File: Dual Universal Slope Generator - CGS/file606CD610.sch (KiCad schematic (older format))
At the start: 81 parts, among them J10 TRIG_IN_B, J11 IN_B, J12 1V/OCT_B, J13 DC_OUT_B, J14 AC_COUPLED_OUT_B, J15 END_OUT_B, J16 BIPOLAR_OUT_B, J22 CV_POT_2_B, J23 FALL_POT_B, J24 RISE_POT_B, J25 SW_RISE_B, J26 SW_FALL_B, J28 LED_B, J9 CV_IN_B, Q10 2N3906, Q11 2N3904, Q12 BC547, Q7 2N3904, Q8 2N3906, Q9 2N3906, SW2 SW_SPDT_MSM, U4 LF353, U5 TL072, U6 LM3900

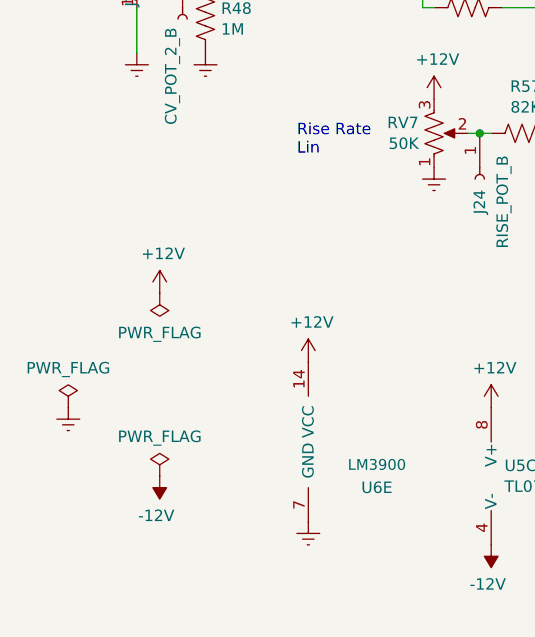
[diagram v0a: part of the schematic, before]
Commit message: added power connectors to DUSG
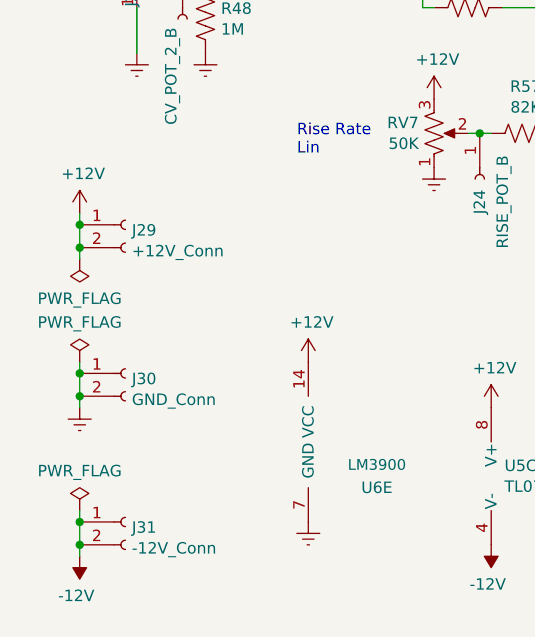
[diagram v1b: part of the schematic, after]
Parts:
- added J29: +12V_Conn, Connector_Wire:SolderWirePad_1x02_P3.81mm_Drill1mm, symbol Connector:Conn_01x02_Female
- added J30: GND_Conn, Connector_Wire:SolderWirePad_1x02_P3.81mm_Drill1mm, symbol Connector:Conn_01x02_Female
- added J31: -12V_Conn, Connector_Wire:SolderWirePad_1x02_P3.81mm_Drill1mm, symbol Connector:Conn_01x02_Female
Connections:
- net +12V: now also J29.1 (Pin_1), J29.2 (Pin_2)
- net -12V: now also J31.1 (Pin_1), J31.2 (Pin_2)
- net Earth: now also J30.1 (Pin_1), J30.2 (Pin_2)
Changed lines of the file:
@@
 L power:+12V #PWR?
 U 1 1 60B184EF
-P 1200 6250
+P 850 5900
 AR Path="/60B184EF" Ref="#PWR?"  Part="1"
 AR Path="/606CD611/60B184EF" Ref="#PWR043"  Part="1"
-F 0 "#PWR043" H 1200 6100 50  0001 C CNN
-F 1 "+12V" H 1215 6423 50  0000 C CNN
-F 2 "" H 1200 6250 50  0001 C CNN
-F 3 "" H 1200 6250 50  0001 C CNN
-	1    1200 6250
+F 0 "#PWR043" H 850 5750 50  0001 C CNN
+F 1 "+12V" H 865 6073 50  0000 C CNN
+F 2 "" H 850 5900 50  0001 C CNN
+F 3 "" H 850 5900 50  0001 C CNN
+	1    850  5900
 	1    0    0    -1
 $EndComp
@@
 L power:-12V #PWR?
 U 1 1 60B184F5
-P 1200 7050
+P 850 7400
 AR Path="/60B184F5" Ref="#PWR?"  Part="1"
 AR Path="/606CD611/60B184F5" Ref="#PWR044"  Part="1"
-F 0 "#PWR044" H 1200 7150 50  0001 C CNN
-F 1 "-12V" H 1215 7223 50  0000 C CNN
-F 2 "" H 1200 7050 50  0001 C CNN
-F 3 "" H 1200 7050 50  0001 C CNN
-	1    1200 7050
+F 0 "#PWR044" H 850 7500 50  0001 C CNN
+F 1 "-12V" H 865 7573 50  0000 C CNN
+F 2 "" H 850 7400 50  0001 C CNN
+F 3 "" H 850 7400 50  0001 C CNN
+	1    850  7400
 	-1   0    0    1
 $EndComp
@@
 L power:Earth #PWR?
 U 1 1 60B184FB
-P 800 6750
+P 850 6750
 AR Path="/60B184FB" Ref="#PWR?"  Part="1"
 AR Path="/606CD611/60B184FB" Ref="#PWR033"  Part="1"
-F 0 "#PWR033" H 800 6500 50  0001 C CNN
-F 1 "Earth" H 800 6600 50  0001 C CNN
-F 2 "" H 800 6750 50  0001 C CNN
-F 3 "~" H 800 6750 50  0001 C CNN
-	1    800  6750
+F 0 "#PWR033" H 850 6500 50  0001 C CNN
+F 1 "Earth" H 850 6600 50  0001 C CNN
+F 2 "" H 850 6750 50  0001 C CNN
+F 3 "~" H 850 6750 50  0001 C CNN
+	1    850  6750
 	1    0    0    -1
 $EndComp
@@
 L power:PWR_FLAG #FLG?
 U 1 1 60B18501
-P 800 6750
+P 850 6550
 AR Path="/60B18501" Ref="#FLG?"  Part="1"
 AR Path="/606CD611/60B18501" Ref="#FLG04"  Part="1"
-F 0 "#FLG04" H 800 6825 50  0001 C CNN
-F 1 "PWR_FLAG" H 800 6923 50  0000 C CNN
-F 2 "" H 800 6750 50  0001 C CNN
-F 3 "~" H 800 6750 50  0001 C CNN
-	1    800  6750
+F 0 "#FLG04" H 850 6625 50  0001 C CNN
+F 1 "PWR_FLAG" H 850 6723 50  0000 C CNN
+F 2 "" H 850 6550 50  0001 C CNN
+F 3 "~" H 850 6550 50  0001 C CNN
+	1    850  6550
 	1    0    0    -1
 $EndComp
@@
 L power:PWR_FLAG #FLG?
 U 1 1 60B18508
-P 1200 7050
+P 850 7200
 AR Path="/60B18508" Ref="#FLG?"  Part="1"
 AR Path="/606CD611/60B18508" Ref="#FLG06"  Part="1"
-F 0 "#FLG06" H 1200 7125 50  0001 C CNN
-F 1 "PWR_FLAG" H 1200 7223 50  0000 C CNN
-F 2 "" H 1200 7050 50  0001 C CNN
-F 3 "~" H 1200 7050 50  0001 C CNN
-	1    1200 7050
+F 0 "#FLG06" H 850 7275 50  0001 C CNN
+F 1 "PWR_FLAG" H 850 7373 50  0000 C CNN
+F 2 "" H 850 7200 50  0001 C CNN
+F 3 "~" H 850 7200 50  0001 C CNN
+	1    850  7200
 	1    0    0    -1
 $EndComp
@@
 L power:PWR_FLAG #FLG?
 U 1 1 60B1850E
-P 1200 6250
+P 850 6100
 AR Path="/60B1850E" Ref="#FLG?"  Part="1"
 AR Path="/606CD611/60B1850E" Ref="#FLG05"  Part="1"
-F 0 "#FLG05" H 1200 6325 50  0001 C CNN
-F 1 "PWR_FLAG" H 1200 6423 50  0000 C CNN
-F 2 "" H 1200 6250 50  0001 C CNN
-F 3 "~" H 1200 6250 50  0001 C CNN
-	1    1200 6250
+F 0 "#FLG05" H 850 6175 50  0001 C CNN
+F 1 "PWR_FLAG" H 850 6273 50  0000 C CNN
+F 2 "" H 850 6100 50  0001 C CNN
+F 3 "~" H 850 6100 50  0001 C CNN
+	1    850  6100
 	-1   0    0    1
 $EndComp
@@
 $EndComp
 Connection ~ 6900 5350
+$Comp
+L Connector:Conn_01x02_Female J29
+U 1 1 6142F65B
+P 1050 5950
+F 0 "J29" H 1078 5926 50  0000 L CNN
+F 1 "+12V_Conn" H 1078 5835 50  0000 L CNN
+F 2 "Connector_Wire:SolderWirePad_1x02_P3.81mm_Drill1mm" H 1050 5950 50  0001 C CNN
+F 3 "~" H 1050 5950 50  0001 C CNN
+	1    1050 5950
+	1    0    0    -1
+$EndComp
+Wire Wire Line
+	850  5900 850  5950
+Wire Wire Line
+	850  6050 850  6100
+Wire Wire Line
+	850  5950 850  6050
+Connection ~ 850  5950
+Connection ~ 850  6050
+Wire Wire Line
+	850  6750 850  6700
+Wire Wire Line
+	850  7400 850  7350
+$Comp
+L Connector:Conn_01x02_Female J30
+U 1 1 6149F7E5
+P 1050 6600
+F 0 "J30" H 1078 6576 50  0000 L CNN
+F 1 "GND_Conn" H 1078 6485 50  0000 L CNN
+F 2 "Connector_Wire:SolderWirePad_1x02_P3.81mm_Drill1mm" H 1050 6600 50  0001 C CNN
+F 3 "~" H 1050 6600 50  0001 C CNN
+	1    1050 6600
+	1    0    0    -1
+$EndComp
+Wire Wire Line
+	850  6600 850  6550
+$Comp
+L Connector:Conn_01x02_Female J31
+U 1 1 6149FF6C
+P 1050 7250
+F 0 "J31" H 1078 7226 50  0000 L CNN
+F 1 "-12V_Conn" H 1078 7135 50  0000 L CNN
+F 2 "Connector_Wire:SolderWirePad_1x02_P3.81mm_Drill1mm" H 1050 7250 50  0001 C CNN
+F 3 "~" H 1050 7250 50  0001 C CNN
+	1    1050 7250
+	1    0    0    -1
+$EndComp
+Wire Wire Line
+	850  7250 850  7200
+Wire Wire Line
+	850  7250 850  7350
+Connection ~ 850  7250
+Connection ~ 850  7350
+Wire Wire Line
+	850  6700 850  6600
+Connection ~ 850  6700
+Connection ~ 850  6600
 $EndSCHEMATC
